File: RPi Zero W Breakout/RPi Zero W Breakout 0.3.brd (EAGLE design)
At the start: 90 x 55 mm, 35 parts, among them J1 35RAPC4BHN2

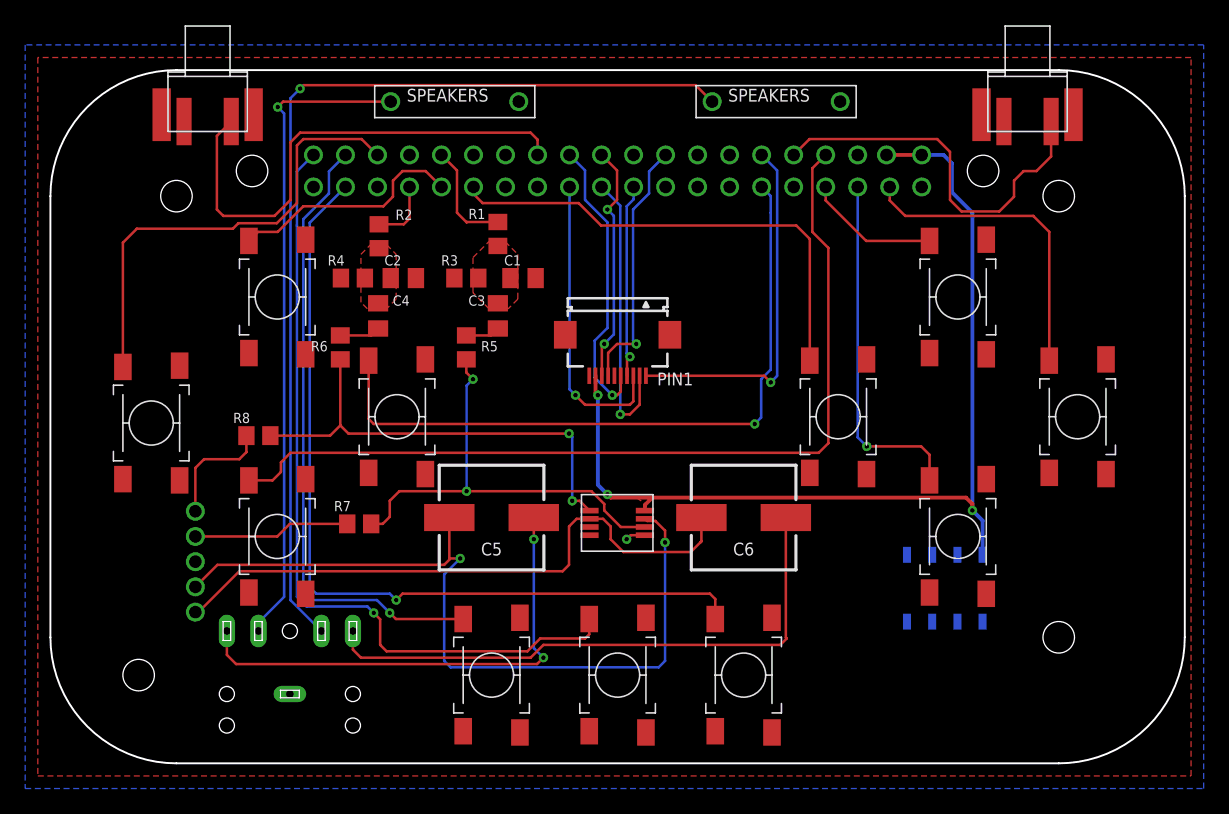
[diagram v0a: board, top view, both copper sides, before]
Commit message: Update
minor layer changes for text
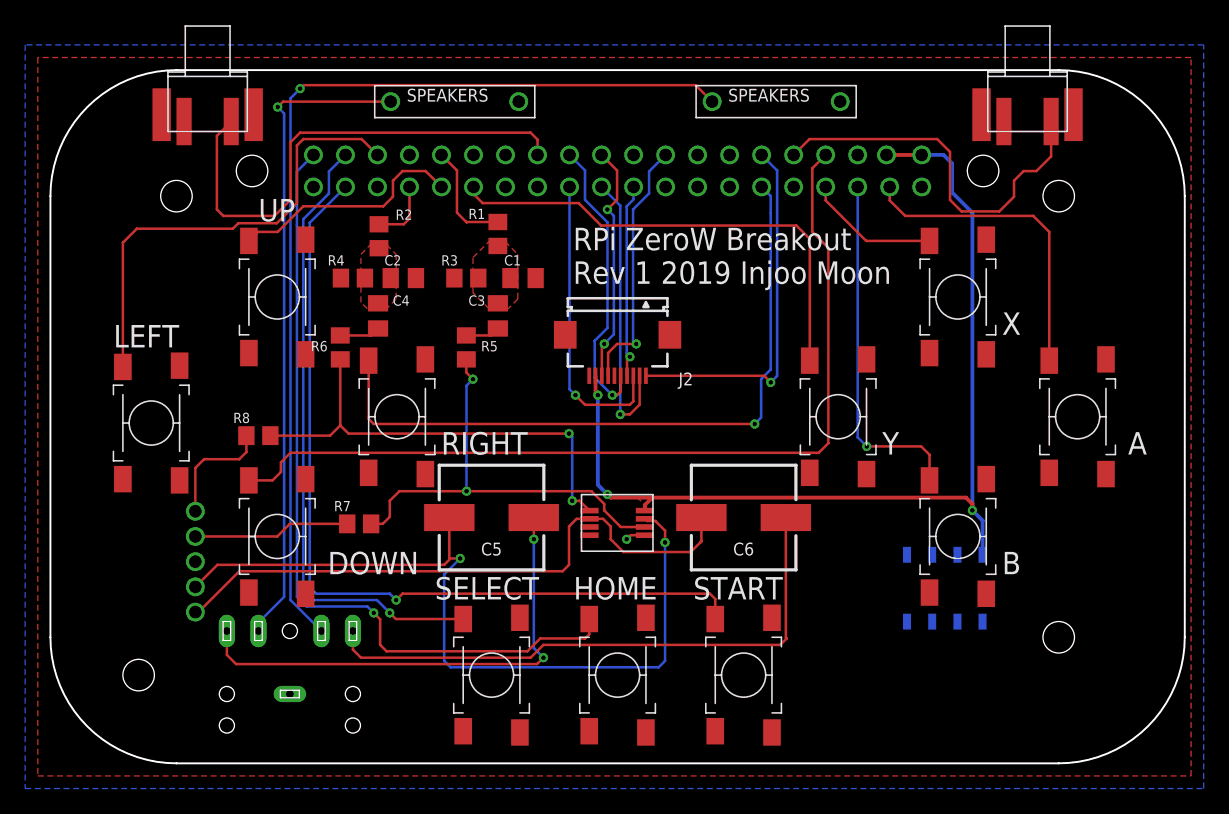
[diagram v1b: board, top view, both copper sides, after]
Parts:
- renumbered PIN1 to J2, U$3 to H1
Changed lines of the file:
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@@
 <wire x1="25" y1="55" x2="25" y2="0" width="0.1524" layer="47"/>
 <wire x1="90" y1="10" x2="0" y2="10" width="0.1524" layer="47"/>
-<wire x1="0" y1="45" x2="10.254" y2="45" width="0.1524" layer="47"/>
 <hole x="10" y="45" drill="2.5"/>
 <hole x="7" y="7" drill="2.5"/>
@@
 <hole x="80" y="45" drill="2.5"/>
 <text x="3.5" y="24" size="1.778" layer="26" rot="MR0">Rf</text>
-<text x="85.5" y="24.5" size="1.778" layer="27">A</text>
-<text x="75.5" y="15" size="1.778" layer="27">B</text>
-<text x="75.5" y="34" size="1.778" layer="27">X</text>
-<text x="66" y="24.5" size="1.778" layer="27">Y</text>
-<text x="51" y="13" size="1.778" layer="27">START</text>
-<text x="41.5" y="13" size="1.778" layer="27">HOME</text>
-<text x="30.5" y="13" size="1.778" layer="27">SELECT</text>
-<text x="16.5" y="43" size="1.778" layer="27">UP</text>
-<text x="22" y="15" size="1.778" layer="27">DOWN</text>
-<text x="5" y="33" size="1.778" layer="27">LEFT</text>
-<text x="31" y="24.5" size="1.778" layer="27">RIGHT</text>
-<text x="59.5" y="3.5" size="1.778" layer="27">RPi ZeroW Breakout
+<text x="85.5" y="24.5" size="1.778" layer="25">A</text>
+<text x="75.5" y="15" size="1.778" layer="25">B</text>
+<text x="75.5" y="34" size="1.778" layer="25">X</text>
+<text x="66" y="24.5" size="1.778" layer="25">Y</text>
+<text x="51" y="13" size="1.778" layer="25">START</text>
+<text x="41.5" y="13" size="1.778" layer="25">HOME</text>
+<text x="30.5" y="13" size="1.778" layer="25">SELECT</text>
+<text x="16.5" y="43" size="1.778" layer="25">UP</text>
+<text x="22" y="15" size="1.778" layer="25">DOWN</text>
+<text x="5" y="33" size="1.778" layer="25">LEFT</text>
+<text x="31" y="24.5" size="1.778" layer="25">RIGHT</text>
+<text x="41.466" y="38.044" size="1.778" layer="25">RPi ZeroW Breakout
 Rev 1 2019 Injoo Moon</text>
-<wire x1="10.254" y1="45" x2="90.254" y2="45" width="0.1524" layer="47"/>
+<wire x1="0" y1="45" x2="90.254" y2="45" width="0.1524" layer="47"/>
 </plain>
 <attributes>
@@
 </autorouter>
 <elements>
-<element name="PIN1" library="con-hirose" library_urn="urn:adsk.eagle:library:152" package="FH12-10S-0.5SH" package3d_urn="urn:adsk.eagle:package:7323/1" value="FH12-10S-0.5SH" x="45" y="34" smashed="yes" rot="R180">
+<element name="J2" library="con-hirose" library_urn="urn:adsk.eagle:library:152" package="FH12-10S-0.5SH" package3d_urn="urn:adsk.eagle:package:7323/1" value="FH12-10S-0.5SH" x="45" y="34" smashed="yes" rot="R180">
 <attribute name="MF" value="" x="19.6" y="68.29" size="1.778" layer="27" rot="R180" display="off"/>
 <attribute name="MPN" value="FH12-10S-0.5SH(55)" x="19.6" y="68.29" size="1.778" layer="27" rot="R180" display="off"/>
@@
 <attribute name="VALUE" x="34.5" y="43" size="0.8128" layer="27" rot="R180"/>
 </element>
-<element name="U$3" library="M22-6340442" package="M22-6340442" value="M22-6340442" x="70.5" y="14" smashed="yes" rot="MR270">
+<element name="H1" library="M22-6340442" package="M22-6340442" value="M22-6340442" x="70.5" y="14" smashed="yes" rot="MR270">
 <attribute name="NAME" x="75" y="11" size="1.016" layer="26" rot="MR180"/>
 </element>
@@
 <signals>
 <signal name="LEDK">
-<contactref element="PIN1" pad="1"/>
+<contactref element="J2" pad="1"/>
 <contactref element="U$1" pad="12"/>
 <wire x1="56.43" y1="48.27" x2="57.658" y2="47.042" width="0.2032" layer="16"/>
@@
 </signal>
 <signal name="MISO">
-<contactref element="PIN1" pad="2"/>
+<contactref element="J2" pad="2"/>
 <contactref element="U$1" pad="21"/>
 <wire x1="43.73" y1="45.73" x2="45.212" y2="44.248" width="0.2032" layer="16"/>
@@
 </signal>
 <signal name="CS">
-<contactref element="PIN1" pad="5"/>
+<contactref element="J2" pad="5"/>
 <contactref element="U$1" pad="24"/>
 <wire x1="45.25" y1="30.75" x2="45.25" y2="29.502" width="0.2032" layer="1"/>
@@
 </signal>
 <signal name="RESET">
-<contactref element="PIN1" pad="8"/>
+<contactref element="J2" pad="8"/>
 <contactref element="U$1" pad="22"/>
 <wire x1="43.73" y1="48.27" x2="44.958" y2="47.042" width="0.2032" layer="1"/>
@@
 <signal name="5V">
 <contactref element="U$2" pad="VDD"/>
-<contactref element="PIN1" pad="9"/>
+<contactref element="J2" pad="9"/>
 <contactref element="U$1" pad="2"/>
 <contactref element="U$1" pad="4"/>
-<contactref element="U$3" pad="P4"/>
+<contactref element="H1" pad="P4"/>
 <wire x1="73.96" y1="16.54" x2="73.96" y2="19.258" width="0.3048" layer="16"/>
 <wire x1="73.96" y1="19.258" x2="73.152" y2="20.066" width="0.3048" layer="16"/>
@@
 </signal>
 <signal name="GND">
-<contactref element="PIN1" pad="10"/>
+<contactref element="J2" pad="10"/>
 <contactref element="C2" pad="2"/>
 <contactref element="R4" pad="1"/>
@@
 <contactref element="U$1" pad="34"/>
 <contactref element="U$1" pad="39"/>
-<contactref element="U$3" pad="P3"/>
+<contactref element="H1" pad="P3"/>
 <polygon width="0.1524" layer="1" rank="6">
 <vertex x="-1" y="-1"/>
@@
 <signal name="MOSI">
 <contactref element="U$1" pad="19"/>
-<contactref element="PIN1" pad="4"/>
+<contactref element="J2" pad="4"/>
 <wire x1="46.27" y1="45.73" x2="46.27" y2="44.746" width="0.2032" layer="16"/>
 <wire x1="46.27" y1="44.746" x2="45.72" y2="44.196" width="0.2032" layer="16"/>
@@
 <signal name="CLK">
 <contactref element="U$1" pad="23"/>
-<contactref element="PIN1" pad="3"/>
+<contactref element="J2" pad="3"/>
 <wire x1="41.19" y1="45.73" x2="41.19" y2="29.676" width="0.2032" layer="16"/>
 <wire x1="41.19" y1="29.676" x2="41.656" y2="29.21" width="0.2032" layer="16"/>
@@
 <signal name="RS/DC">
 <contactref element="U$1" pad="18"/>
-<contactref element="PIN1" pad="7"/>
+<contactref element="J2" pad="7"/>
 <wire x1="44.25" y1="30.75" x2="44.25" y2="32.566" width="0.2032" layer="1"/>
 <wire x1="44.25" y1="32.566" x2="44.958" y2="33.274" width="0.2032" layer="1"/>
